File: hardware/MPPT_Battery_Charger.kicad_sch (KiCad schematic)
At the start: 74 parts, among them Q24 SI7414DN-T1-E3, Q25 SI7414DN-T1-E3, Q5 SI2302DDS-T1-GE3, Q5 SI7414DN-T1-E3, Q6 SI7414DN-T1-E3, U22 BQ24650RVAT, U26 LMV321RIYLT, U28 LMV321RIYLT, U4 INA199C1DCKR

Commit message: hardware: starting the pcb project
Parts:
- removed Q5 (x2): SI2302DDS-T1-GE3, footprints:SI2302DDS-T1-GE3, symbol SI2302DDS-T1-GE3:SI2302DDS-T1-GE3
- added Q8 (x2): SI2302DDS-T1-GE3, footprints:SI2302DDS-T1-GE3, symbol SI2302DDS-T1-GE3:SI2302DDS-T1-GE3
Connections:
- net BC_A_~{EN}: now also Q8.1 (G)
- net BC_B_~{EN}: now also Q8.1 (G)
- net GND: now also Q8.2 (S), Q8.2 (S)
- net at R104.1, R87.2, U22.2 (MPPSET): now also Q8.3 (D)
- net at R104.1, R91.2, U22.2 (MPPSET): now also Q8.3 (D)
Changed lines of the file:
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@@
     )
   )
+  (symbol (lib_id "SI2302DDS-T1-GE3:SI2302DDS-T1-GE3") (at 116.84 147.32 0) (unit 1)
+    (in_bom yes) (on_board yes) (dnp no)
+    (property "Reference" "Q8" (at 128.27 147.32 90)
+      (effects (font (size 1.27 1.27)) (justify left))
+    )
+    (property "Value" "SI2302DDS-T1-GE3" (at 130.81 157.48 90)
+      (effects (font (size 1.27 1.27)) (justify left))
+    )
+    (property "Footprint" "footprints:SI2302DDS-T1-GE3" (at 105.41 181.61 0)
+      (effects (font (size 1.27 1.27)) (justify left top) hide)
+    )
+    (property "Datasheet" "http://www.vishay.com/docs/63653/si2302dds.pdf" (at 92.456 184.404 0)
+      (effects (font (size 1.27 1.27)) (justify left top) hide)
+    )
+    (property "Height" "1.12" (at 128.27 546.05 0)
+      (effects (font (size 1.27 1.27)) (justify left top) hide)
+    )
+    (property "Mouser Part Number" "78-SI2302DDS-T1-GE3" (at 128.27 646.05 0)
+      (effects (font (size 1.27 1.27)) (justify left top) hide)
+    )
+    (property "Mouser Price/Stock" "https://www.mouser.co.uk/ProductDetail/Vishay-Semiconductors/SI2302DDS-T1-GE3?qs=MxnWX8BLHKdaCSNWhg%252BxLA%3D%3D" (at 128.27 746.05 0)
+      (effects (font (size 1.27 1.27)) (justify left top) hide)
+    )
+    (property "Manufacturer_Name" "Vishay" (at 128.27 846.05 0)
+      (effects (font (size 1.27 1.27)) (justify left top) hide)
+    )
+    (property "Manufacturer_Part_Number" "SI2302DDS-T1-GE3" (at 128.27 946.05 0)
+      (effects (font (size 1.27 1.27)) (justify left top) hide)
+    )
+    (pin "1")
+    (pin "2")
+    (pin "3")
+    (instances
+      (project "eps-re_project"
+        (path "/2eebaa11-d7ed-4bfd-bc8e-988f68654d29/6f34948c-43a8-4614-b8ed-90c5b6b9b243"
+          (reference "Q8") (unit 1)
+        )
+        (path "/2eebaa11-d7ed-4bfd-bc8e-988f68654d29/0b69622c-4960-45c0-904b-657ff8db02ea"
+          (reference "Q10") (unit 1)
+        )
+      )
+    )
+  )
   (symbol (lib_id "power:PWR_FLAG") (at 347.98 240.03 0) (unit 1)
     (in_bom yes) (on_board yes) (dnp no) (fields_autoplaced)
@@
     )
   )
-  (symbol (lib_id "SI2302DDS-T1-GE3:SI2302DDS-T1-GE3") (at 116.84 41.91 0) (unit 1)
-    (in_bom yes) (on_board yes) (dnp no)
-    (property "Reference" "Q5" (at 118.11 34.29 0)
-      (effects (font (size 1.27 1.27)) (justify left))
-    )
-    (property "Value" "SI2302DDS-T1-GE3" (at 118.7439 36.83 90)
-      (effects (font (size 1.27 1.27)) (justify left) hide)
-    )
-    (property "Footprint" "footprints:SI2302DDS-T1-GE3" (at 105.41 76.2 0) (show_name)
-      (effects (font (size 1.27 1.27)) (justify left top) hide)
-    )
-    (property "Datasheet" "http://www.vishay.com/docs/63653/si2302dds.pdf" (at 92.456 78.994 0) (show_name)
-      (effects (font (size 1.27 1.27)) (justify left top) hide)
-    )
-    (property "Height" "1.12" (at 128.27 440.64 0)
-      (effects (font (size 1.27 1.27)) (justify left top) hide)
-    )
-    (property "Mouser Part Number" "78-SI2302DDS-T1-GE3" (at 128.27 540.64 0)
-      (effects (font (size 1.27 1.27)) (justify left top) hide)
-    )
-    (property "Mouser Price/Stock" "https://www.mouser.co.uk/ProductDetail/Vishay-Semiconductors/SI2302DDS-T1-GE3?qs=MxnWX8BLHKdaCSNWhg%252BxLA%3D%3D" (at 128.27 640.64 0)
-      (effects (font (size 1.27 1.27)) (justify left top) hide)
-    )
-    (property "Manufacturer_Name" "Vishay" (at 128.27 740.64 0)
-      (effects (font (size 1.27 1.27)) (justify left top) hide)
-    )
-    (property "Manufacturer_Part_Number" "SI2302DDS-T1-GE3" (at 128.27 840.64 0)
-      (effects (font (size 1.27 1.27)) (justify left top) hide)
-    )
-    (pin "1")
-    (pin "2")
-    (pin "3")
-    (instances
-      (project "eps-re_project"
-        (path "/2eebaa11-d7ed-4bfd-bc8e-988f68654d29/6f34948c-43a8-4614-b8ed-90c5b6b9b243"
-          (reference "Q5") (unit 1)
-        )
-        (path "/2eebaa11-d7ed-4bfd-bc8e-988f68654d29/0b69622c-4960-45c0-904b-657ff8db02ea"
-          (reference "Q15") (unit 1)
-        )
-      )
-      (project "EPSpg3"
-        (path "/95ab2aaf-8d7f-4e6e-818d-723704a56097"
-          (reference "Q2") (unit 1)
-        )
-      )
-    )
-  )
   (symbol (lib_id "power:GND") (at 223.52 186.69 0) (unit 1)
     (in_bom yes) (on_board yes) (dnp no) (fields_autoplaced)
@@
     )
   )
-  (symbol (lib_id "SI2302DDS-T1-GE3:SI2302DDS-T1-GE3") (at 116.84 147.32 0) (unit 1)
-    (in_bom yes) (on_board yes) (dnp no)
-    (property "Reference" "Q5" (at 118.11 139.7 0)
-      (effects (font (size 1.27 1.27)) (justify left))
-    )
-    (property "Value" "SI2302DDS-T1-GE3" (at 118.7439 142.24 90)
-      (effects (font (size 1.27 1.27)) (justify left) hide)
-    )
-    (property "Footprint" "footprints:SI2302DDS-T1-GE3" (at 105.41 181.61 0) (show_name)
-      (effects (font (size 1.27 1.27)) (justify left top) hide)
-    )
-    (property "Datasheet" "http://www.vishay.com/docs/63653/si2302dds.pdf" (at 92.456 184.404 0) (show_name)
-      (effects (font (size 1.27 1.27)) (justify left top) hide)
-    )
-    (property "Height" "1.12" (at 128.27 546.05 0)
-      (effects (font (size 1.27 1.27)) (justify left top) hide)
-    )
-    (property "Mouser Part Number" "78-SI2302DDS-T1-GE3" (at 128.27 646.05 0)
-      (effects (font (size 1.27 1.27)) (justify left top) hide)
-    )
-    (property "Mouser Price/Stock" "https://www.mouser.co.uk/ProductDetail/Vishay-Semiconductors/SI2302DDS-T1-GE3?qs=MxnWX8BLHKdaCSNWhg%252BxLA%3D%3D" (at 128.27 746.05 0)
-      (effects (font (size 1.27 1.27)) (justify left top) hide)
-    )
-    (property "Manufacturer_Name" "Vishay" (at 128.27 846.05 0)
-      (effects (font (size 1.27 1.27)) (justify left top) hide)
-    )
-    (property "Manufacturer_Part_Number" "SI2302DDS-T1-GE3" (at 128.27 946.05 0)
-      (effects (font (size 1.27 1.27)) (justify left top) hide)
-    )
-    (pin "1")
-    (pin "2")
-    (pin "3")
-    (instances
-      (project "eps-re_project"
-        (path "/2eebaa11-d7ed-4bfd-bc8e-988f68654d29/6f34948c-43a8-4614-b8ed-90c5b6b9b243"
-          (reference "Q5") (unit 1)
-        )
-        (path "/2eebaa11-d7ed-4bfd-bc8e-988f68654d29/0b69622c-4960-45c0-904b-657ff8db02ea"
-          (reference "Q17") (unit 1)
-        )
-      )
-      (project "EPSpg3"
-        (path "/95ab2aaf-8d7f-4e6e-818d-723704a56097"
-          (reference "Q2") (unit 1)
-        )
-      )
-    )
-  )
   (symbol (lib_id "LTST-C190GKT:LTST-C190GKT") (at 137.16 96.52 0) (unit 1)
     (in_bom yes) (on_board yes) (dnp no)
@@
         )
       )
+    )
+  )
+  (symbol (lib_id "SI2302DDS-T1-GE3:SI2302DDS-T1-GE3") (at 116.84 41.91 0) (unit 1)
+    (in_bom yes) (on_board yes) (dnp no)
+    (property "Reference" "Q8" (at 128.27 41.91 90)
+      (effects (font (size 1.27 1.27)) (justify left))
+    )
+    (property "Value" "SI2302DDS-T1-GE3" (at 130.81 52.07 90)
+      (effects (font (size 1.27 1.27)) (justify left))
+    )
+    (property "Footprint" "footprints:SI2302DDS-T1-GE3" (at 105.41 76.2 0)
+      (effects (font (size 1.27 1.27)) (justify left top) hide)
+    )
+    (property "Datasheet" "http://www.vishay.com/docs/63653/si2302dds.pdf" (at 92.456 78.994 0)
+      (effects (font (size 1.27 1.27)) (justify left top) hide)
+    )
+    (property "Height" "1.12" (at 128.27 440.64 0)
+      (effects (font (size 1.27 1.27)) (justify left top) hide)
+    )
+    (property "Mouser Part Number" "78-SI2302DDS-T1-GE3" (at 128.27 540.64 0)
+      (effects (font (size 1.27 1.27)) (justify left top) hide)
+    )
+    (property "Mouser Price/Stock" "https://www.mouser.co.uk/ProductDetail/Vishay-Semiconductors/SI2302DDS-T1-GE3?qs=MxnWX8BLHKdaCSNWhg%252BxLA%3D%3D" (at 128.27 640.64 0)
+      (effects (font (size 1.27 1.27)) (justify left top) hide)
+    )
+    (property "Manufacturer_Name" "Vishay" (at 128.27 740.64 0)
+      (effects (font (size 1.27 1.27)) (justify left top) hide)
+    )
+    (property "Manufacturer_Part_Number" "SI2302DDS-T1-GE3" (at 128.27 840.64 0)
+      (effects (font (size 1.27 1.27)) (justify left top) hide)
+    )
+    (pin "1")
+    (pin "2")
+    (pin "3")
+    (instances
+      (project "eps-re_project"
+        (path "/2eebaa11-d7ed-4bfd-bc8e-988f68654d29/6f34948c-43a8-4614-b8ed-90c5b6b9b243"
+          (reference "Q8") (unit 1)
+        )
+        (path "/2eebaa11-d7ed-4bfd-bc8e-988f68654d29/0b69622c-4960-45c0-904b-657ff8db02ea"
+          (reference "Q13") (unit 1)
+        )
+      )

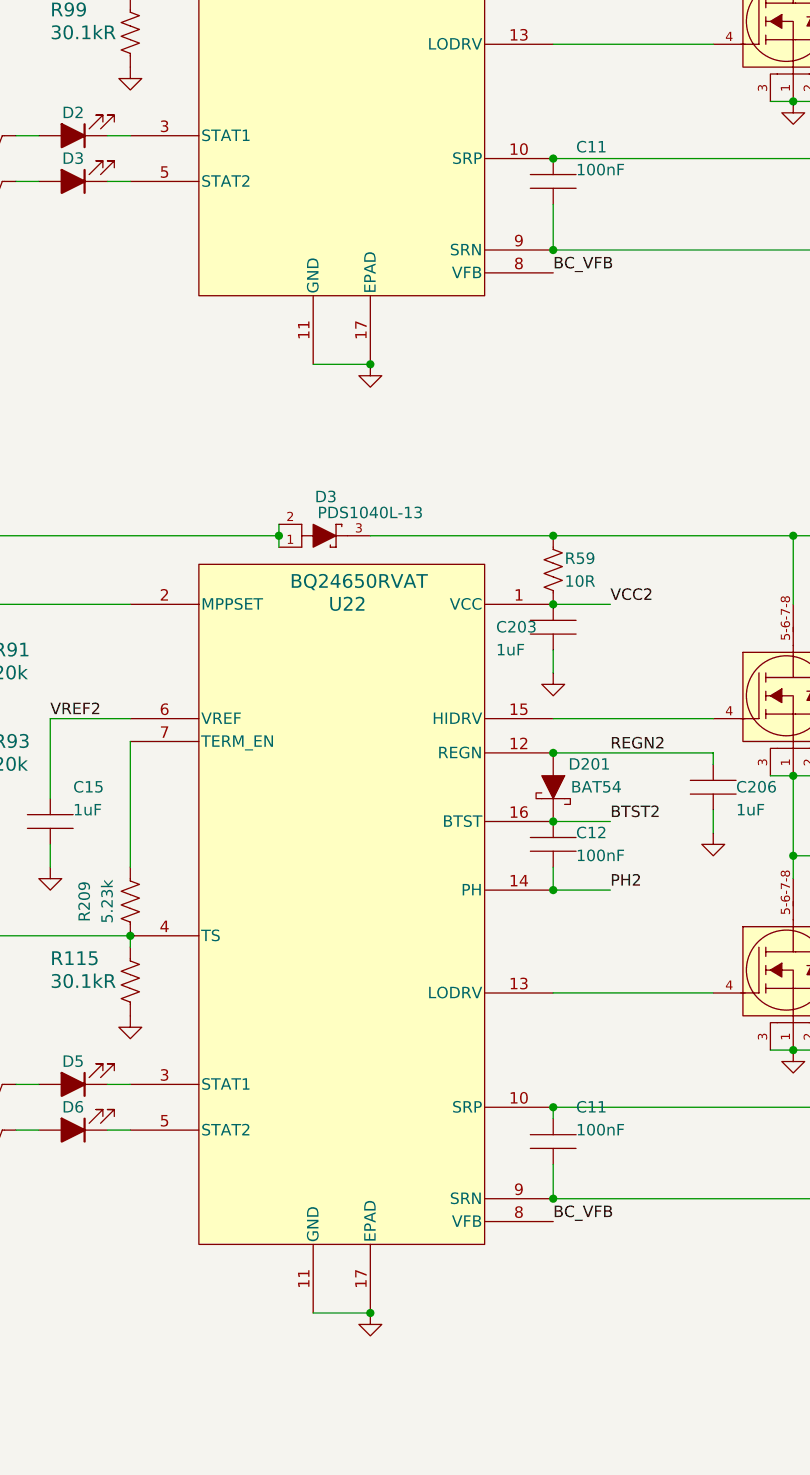
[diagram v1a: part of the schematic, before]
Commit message: hardware: Updating the BQ24650RVAT footprint.
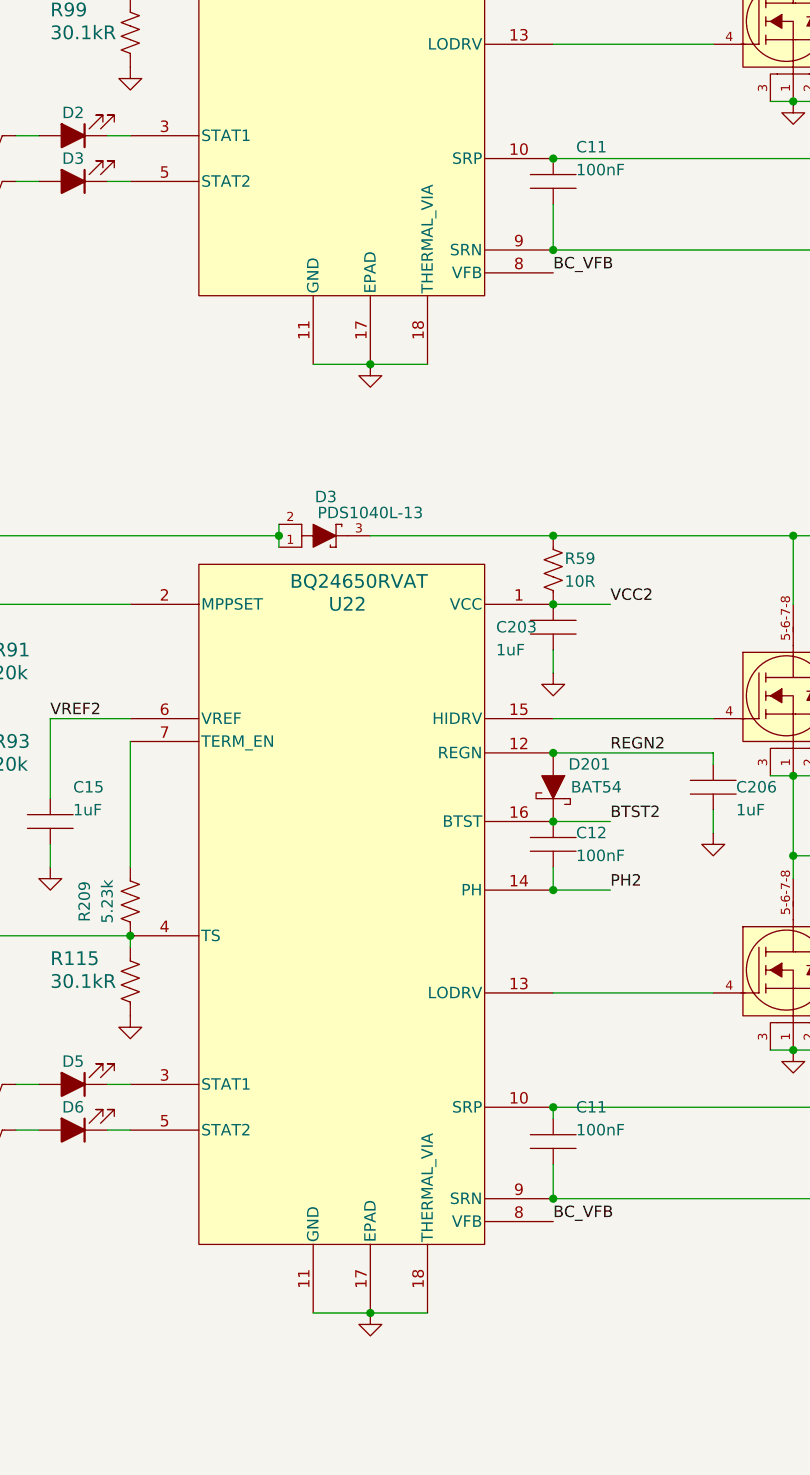
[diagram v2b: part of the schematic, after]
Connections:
- net GND: now also U22.18 (THERMAL_VIA), U22.18 (THERMAL_VIA)
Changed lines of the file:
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@@
     (stroke (width 0) (type default))
   )
+  (wire (pts (xy 176.53 110.49) (xy 182.88 110.49))
+    (stroke (width 0) (type default))
+  )
   (wire (pts (xy 134.62 173.99) (xy 149.86 173.99))
     (stroke (width 0) (type default))
@@
     (stroke (width 0) (type default))
   )
+  (wire (pts (xy 176.53 215.9) (xy 182.88 215.9))
+    (stroke (width 0) (type default))
+  )
   (wire (pts (xy 134.62 68.58) (xy 149.86 68.58))
     (stroke (width 0) (type default))
@@
     (pin "11")
     (pin "17")
+    (pin "18")
     (pin "7")
     (instances
@@
     )
   )
-  (symbol (lib_id "BQ24650RVAT:BQ24650RVAT") (at 115.57 134.62 0) (unit 1)
+  (symbol (lib_name "BQ24650RVAT_1") (lib_id "BQ24650RVAT:BQ24650RVAT") (at 115.57 134.62 0) (unit 1)
     (in_bom yes) (on_board yes) (dnp no)
     (property "Reference" "U22" (at 173.99 31.75 0)
@@
     (pin "11")
     (pin "17")
+    (pin "18")
     (pin "7")
     (instances
